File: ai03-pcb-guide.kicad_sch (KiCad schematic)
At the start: 0 parts

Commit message: New Type C Lib and early MCU Schema
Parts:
- added C1: 1uF, symbol Device:C_Small
- added C2, C3, C4, C8: 0.1uF, symbol Device:C_Small
- added C5: 10uF, symbol Device:C_Small
- added C6, C7: 22pF, symbol Device:C_Small
- added J1: AVR-ISP-6, symbol Connector:AVR-ISP-6
- added R1, R4: 10k, symbol Device:R_Small
- added R2, R3: 22, symbol Device:R_Small
- added SW1: SW_Push, symbol Switch:SW_Push
- added U1: ATmega32U4-A, Package_QFP:TQFP-44_10x10mm_P0.8mm, symbol MCU_Microchip_ATmega:ATmega32U4-A
- added Y1: 16MHz, symbol Device:Crystal_GND24_Small
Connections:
- new net: R4.2, SW1.2, U1.13 (~{RESET})
- new net: C1.1, U1.6 (UCAP)
- new net: R1.2, U1.33 (~{HWB}/PE2)
- new net: C6.2, U1.17 (XTAL1), Y1.1
- new net: C7.2, U1.16 (XTAL2), Y1.3
- new net: R3.1, U1.3 (D-)
- new net: R2.2, U1.4 (D+)
- new net +5V: C2.1, C3.1, C4.1, C5.1, C8.1, J1.2 (VCC), R4.1, U1.14 (VCC), U1.2 (UVCC), U1.24 (AVCC), U1.34 (VCC), U1.44 (AVCC), U1.7 (VBUS)
- new net D+: R2.1
- new net D-: R3.2
- new net GND: C1.2, C2.2, C3.2, C4.2, C5.2, C6.1, C7.1, C8.2, J1.6 (GND), R1.1, SW1.1, U1.15 (GND), U1.23 (GND), U1.35 (GND), U1.43 (GND), U1.5 (UGND), Y1.2 (G), Y1.4 (G)
- new net MISO: J1.1 (MISO), U1.11 (PB3)
- new net MOSI: J1.4 (MOSI), U1.10 (PB2)
- new net RESET: J1.5 (~{RST})
- new net SCK: J1.3 (SCK), U1.9 (PB1)

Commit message: more MCU schema
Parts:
- added USB1: HRO-TYPE-C-31-M-12, symbol Type-C:HRO-TYPE-C-31-M-12
- renumbered C8 to C1, C1 to C7, C6 to C8, C7 to C9
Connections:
- net D+: now also R3.1, U1.4 (D+); no longer R2.1
- net D-: now also R2.2, U1.3 (D-); no longer R3.2
- net RESET: now also R4.2, SW1.2, U1.13 (~{RESET})
- net XTAL1: now reaches C8.2, U1.17 (XTAL1), Y1.1
- net XTAL2: now reaches C9.2, U1.16 (XTAL2), Y1.3
- new net: R3.2, USB1.6 (DP1), USB1.8 (DP2)
- new net: R2.1, USB1.5 (DN2), USB1.7 (DN1)
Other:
- moved on the sheet: C7, C8, C9, J1, R1, R2, R3, R4, SW1, U1, Y1

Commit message: MCU schema and matrix schema
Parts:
- added F1: 500m, symbol Device:Polyfuse_Small
- added R5, R6: 5.1k, symbol Device:R_Small
- added U2: PRTR5V0U2X, symbol random-keyboard-parts:PRTR5V0U2X
- renumbered C8 to C1, C9 to C2, C7 to C3, C1 to C4, C2 to C5, C3 to C6, C4 to C7, C5 to C8, R4 to R1, R1 to R2, R2 to R3, R3 to R4
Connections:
- net +5V: now also F1.2
- net GND: now also USB1.1 (GND), USB1.12 (GND), USB1.13 (SHIELD), R5.2, R6.2, U2.1 (GND)
- net MISO: no longer U1.11 (PB3)
- net MOSI: no longer U1.10 (PB2)
- net SCK: no longer U1.9 (PB1)
- net at R4.2, USB1.6 (DP1), USB1.8 (DP2): now also U2.2 (IO1)
- net at R3.1, USB1.5 (DN2), USB1.7 (DN1): now also U2.3 (IO2)
- net at USB1.10 (CC2): now also R5.1
- net VCC: now reaches USB1.11 (VBUS)
- net VCC: now also USB1.2 (VBUS), F1.1, U2.4 (VCC)
- net at USB1.4 (CC1): now also R6.1
- net Row 0: now reaches U1.1 (PE6)
- net Col 7: now reaches U1.18 (PD0)
- net Col 8: now reaches U1.19 (PD1)
- net Col 9: now reaches U1.20 (PD2)
- net Col 10: now reaches U1.21 (PD3)
- net Col 12: now reaches U1.22 (PD5)
- net Col 11: now reaches U1.25 (PD4)
- net Col 13: now reaches U1.26 (PD6)
- net Col 14: now reaches U1.27 (PD7)
- net Col 0: now reaches U1.28 (PB4)
- net Col 1: now reaches U1.29 (PB5)
- net Col 2: now reaches U1.30 (PB6)
- net Col 3: now reaches U1.31 (PC6)
- net Col 4: now reaches U1.32 (PC7)
- net Col 5: now reaches U1.36 (PF7)
- net Row 1: now reaches U1.37 (PF6)
- net Row 5: now reaches U1.38 (PF5)
- net Row 4: now reaches U1.39 (PF4)
- net Row 3: now reaches U1.40 (PF1)
- net Row 2: now reaches U1.41 (PF0)
- net Col 6: now reaches U1.8 (PB0)
- no-connect marks 0 -> 4
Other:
- added sheet matrix (matrix.kicad_sch)
- moved on the sheet: C1, C2, C3, C4, C5, C6, C7, C8, J1, R1, R2, R3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

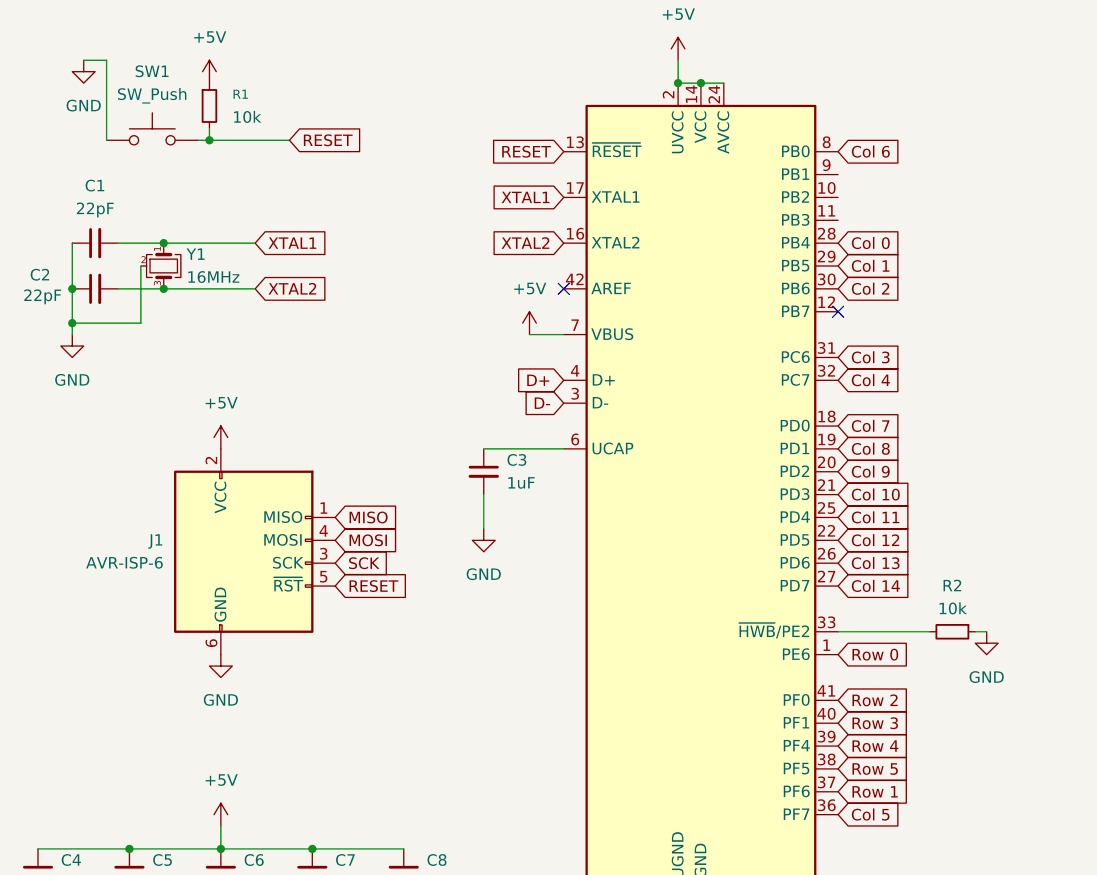
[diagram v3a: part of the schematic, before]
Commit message: schema mostly done with footprints added
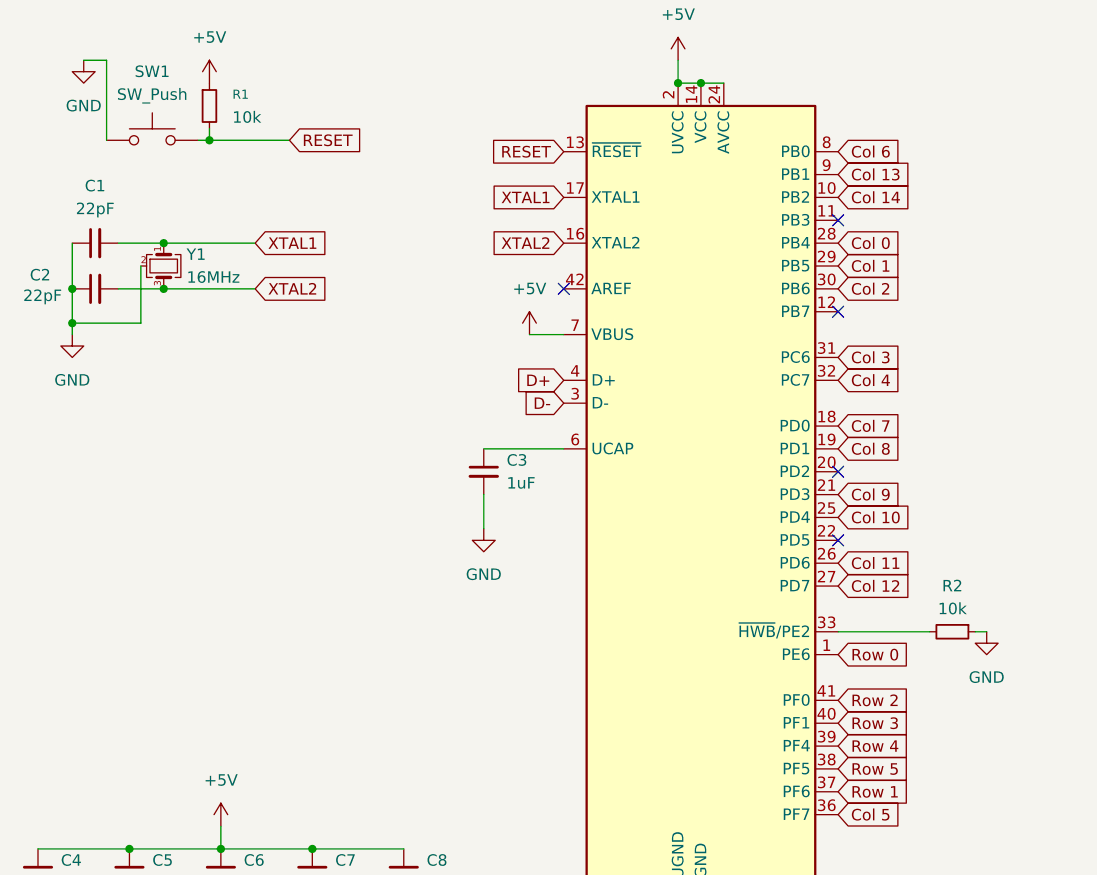
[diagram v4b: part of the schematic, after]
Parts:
- removed J1: AVR-ISP-6, symbol Connector:AVR-ISP-6
- C1, C2, C3, C4, C5, C6, C7: footprint (none) -> Capacitor_SMD:C_0805_2012Metric
- C8: footprint (none) -> Diode_SMD:D_SOD-123
- F1: footprint (none) -> Fuse:Fuse_1206_3216Metric
- R1, R2, R3, R4, R5, R6: footprint (none) -> Resistor_SMD:R_0805_2012Metric
- SW1: footprint (none) -> MX_Only:MXOnly-1U
- U2: footprint (none) -> random-keyboard-parts:SOT143B
- USB1: footprint (none) -> Type-C:HRO-TYPE-C-31-M-12
- Y1: footprint (none) -> Crystal:Crystal_SMD_3225-4Pin_3.2x2.5mm
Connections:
- net Col 10: now also U1.25 (PD4); no longer U1.21 (PD3)
- net Col 11: now also U1.26 (PD6); no longer U1.25 (PD4)
- net Col 12: now also U1.27 (PD7); no longer U1.22 (PD5)
- net Col 13: now also U1.9 (PB1); no longer U1.26 (PD6)
- net Col 14: now also U1.10 (PB2); no longer U1.27 (PD7)
- net Col 9: now also U1.21 (PD3); no longer U1.20 (PD2)
- no-connect marks 4 -> 7

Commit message: schema and pcb changes
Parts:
- SW1: footprint MX_Only:MXOnly-1U -> Button_Switch_SMD:SW_SPST_SKQG_WithStem
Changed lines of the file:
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@@
 			)
 		)
-		(property "Footprint" "MX_Only:MXOnly-1U"
+		(property "Footprint" "Button_Switch_SMD:SW_SPST_SKQG_WithStem"
 			(at 33.02 29.21 0)
 			(hide yes)

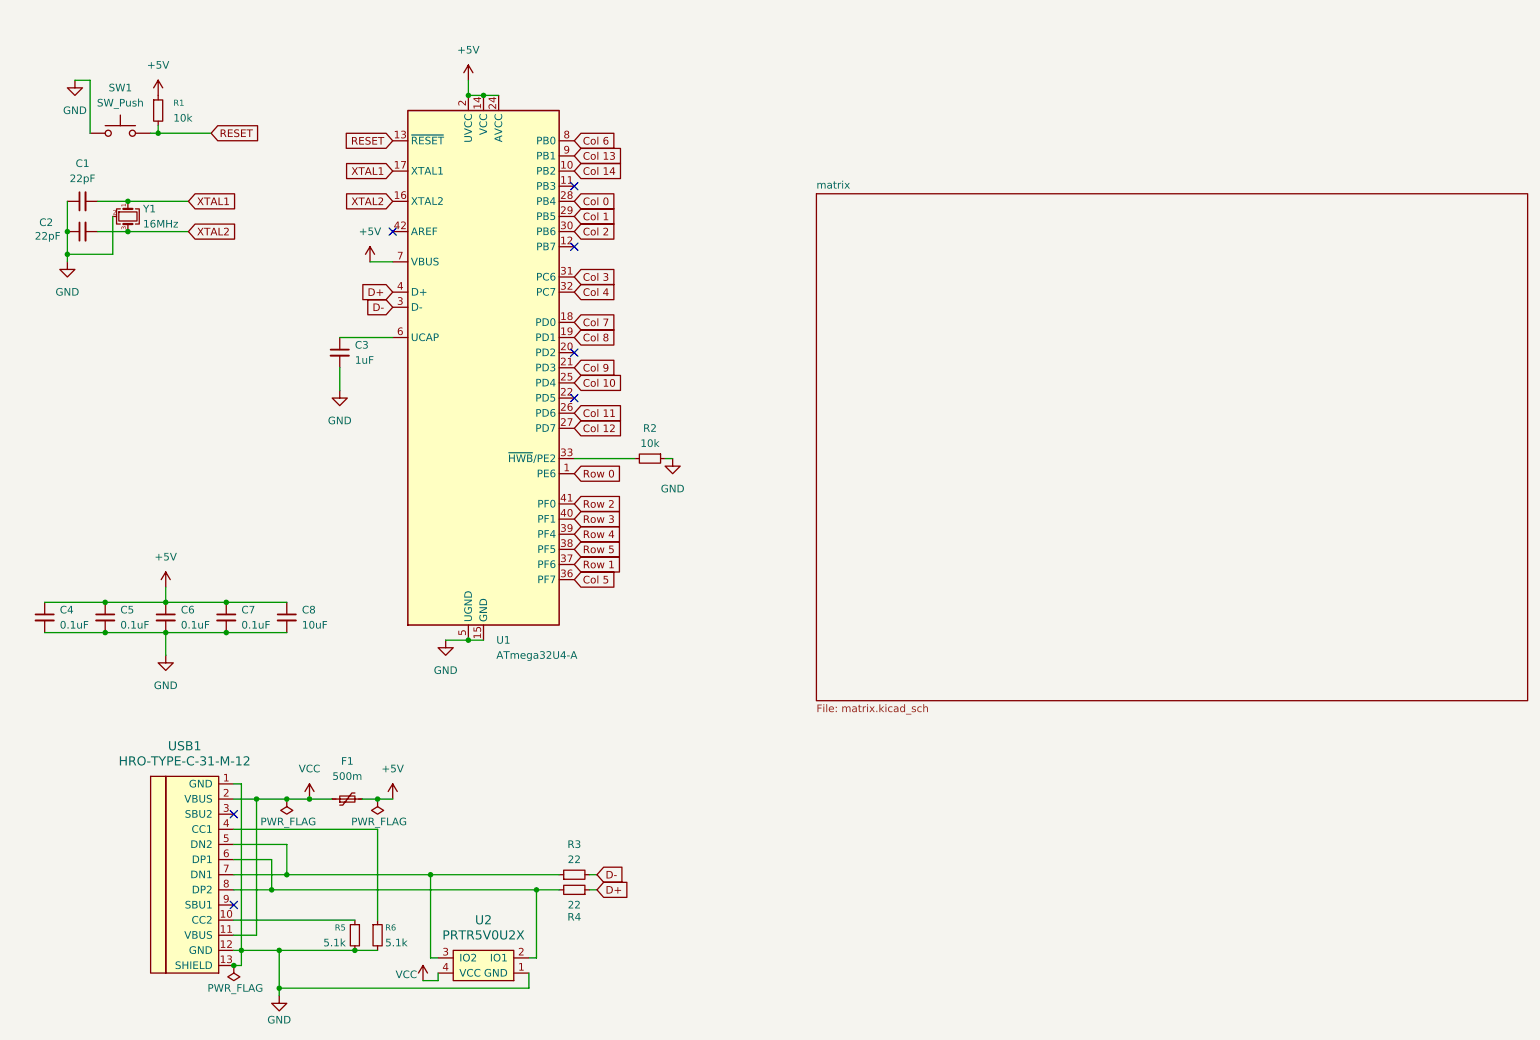
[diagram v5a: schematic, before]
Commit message: pcb finished except for routing
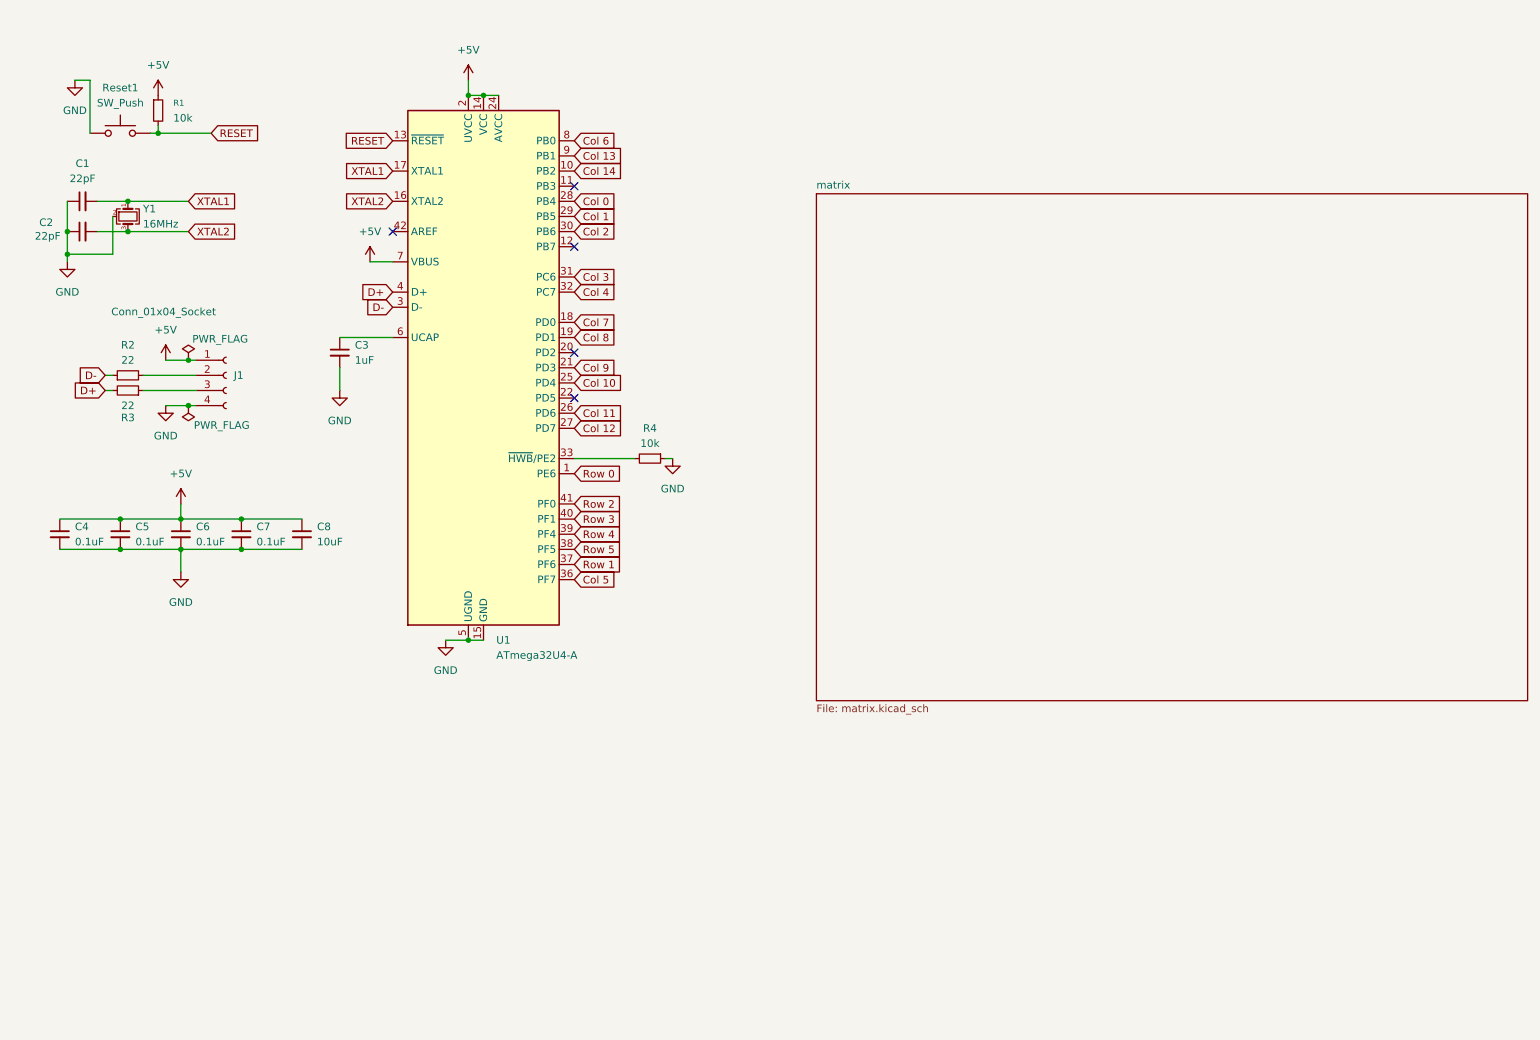
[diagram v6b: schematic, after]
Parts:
- removed F1: 500m, Fuse:Fuse_1206_3216Metric, symbol Device:Polyfuse_Small
- removed R4: 22, Resistor_SMD:R_0805_2012Metric, symbol Device:R_Small
- removed R5, R6: 5.1k, Resistor_SMD:R_0805_2012Metric, symbol Device:R_Small
- removed U2: PRTR5V0U2X, random-keyboard-parts:SOT143B, symbol random-keyboard-parts:PRTR5V0U2X
- removed USB1: HRO-TYPE-C-31-M-12, Type-C:HRO-TYPE-C-31-M-12, symbol Type-C:HRO-TYPE-C-31-M-12
- added J1: Conn_01x04_Socket, Connector_Molex:Molex_Pico-EZmate_78171-0004_1x04-1MP_P1.20mm_Vertical, symbol Connector:Conn_01x04_Socket
- added R2: 22, Resistor_SMD:R_0805_2012Metric, symbol Device:R_Small
- C8: footprint Diode_SMD:D_SOD-123 -> Resistor_SMD:R_0805_2012Metric
- renumbered R2 to R4, SW1 to Reset1
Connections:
- net +5V: now also J1.1 (Pin_1)
- net D+: now also R3.2
- net D-: now also R2.1; no longer R3.2
- net GND: now also J1.4 (Pin_4)
- net at R3.1: now also J1.3 (Pin_3)
- new net: J1.2 (Pin_2), R2.2
- no-connect marks 7 -> 5
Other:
- moved on the sheet: C4, C5, C6, C7, C8
